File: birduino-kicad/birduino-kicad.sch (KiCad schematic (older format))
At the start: 22 parts, among them J1 Conn_01x03_Male, J2 Conn_01x02_Male, J3 Conn_02x05_Odd_Even, J4 Conn_01x04, Q1 2N7000, Q2 2N7000, Q3 2N7000, SW1 SW_Push_Dual, SW2 SW_Push_Dual, SW3 SW_Push_Dual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

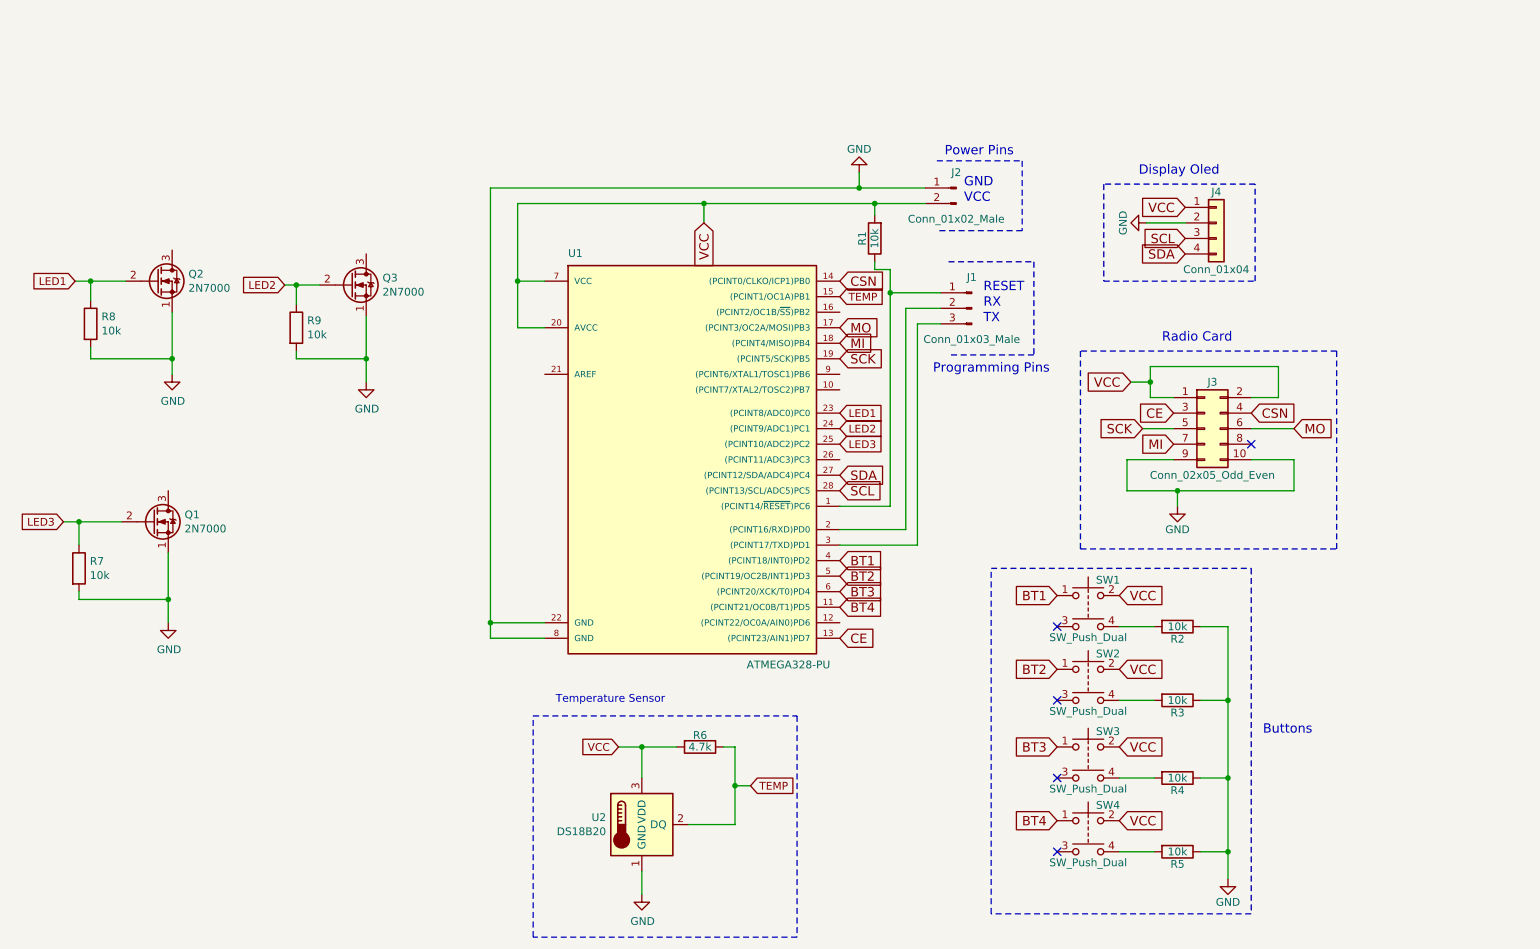
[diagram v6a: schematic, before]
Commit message: feat: add new sensors and components
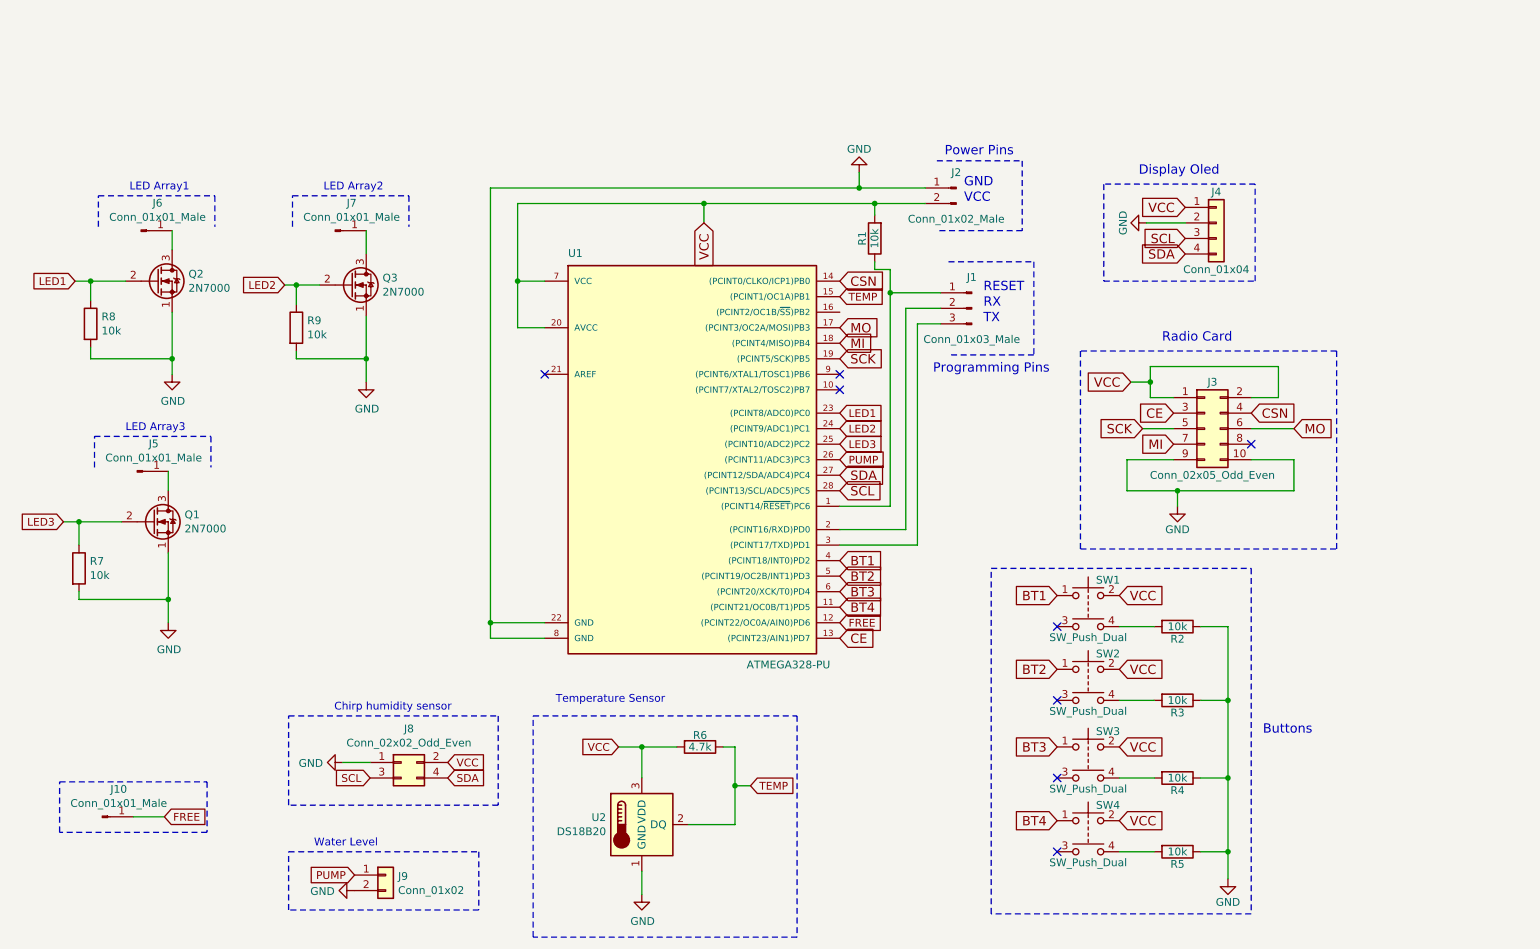
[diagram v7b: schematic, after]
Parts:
- added J10, J5, J6, J7: Conn_01x01_Male, Connector_PinHeader_2.54mm:PinHeader_1x01_P2.54mm_Vertical, symbol Connector:Conn_01x01_Male
- added J8: Conn_02x02_Odd_Even, Connector_PinHeader_2.54mm:PinHeader_2x02_P2.54mm_Vertical, symbol Connector_Generic:Conn_02x02_Odd_Even
- added J9: Conn_01x02, Connector_PinHeader_2.54mm:PinHeader_1x02_P2.54mm_Vertical, symbol Connector_Generic:Conn_01x02
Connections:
- net GND: now also J8.1 (Pin_1), J9.2 (Pin_2)
- net SCL: now also J8.3 (Pin_3)
- net SDA: now also J8.4 (Pin_4)
- net VCC: now also J8.2 (Pin_2)
- net FREE: now reaches U1.12 ((PCINT22/OC0A/AIN0)PD6)
- net FREE: now also J10.1 (Pin_1)
- net PUMP: now reaches U1.26 ((PCINT11/ADC3)PC3)
- net PUMP: now also J9.1 (Pin_1)
- net at Q3.3 (D): now also J7.1 (Pin_1)
- net at Q2.3 (D): now also J6.1 (Pin_1)
- net at Q1.3 (D): now also J5.1 (Pin_1)
- no-connect marks 5 -> 8
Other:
- note added: "Chirp humidity sensor"
- note added: "LED Array1"
- note added: "LED Array2"
- note added: "LED Array3"
- note added: "Water Level"
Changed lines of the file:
@@
 Text GLabel 6525 3275 2    50   Input ~ 0
 LED3
+$Comp
+L Connector:Conn_01x01_Male J6
+U 1 1 5C995BFC
+P 2025 1900
+F 0 "J6" H 2131 2078 50  0000 C CNN
+F 1 "Conn_01x01_Male" H 2131 1987 50  0000 C CNN
+F 2 "Connector_PinHeader_2.54mm:PinHeader_1x01_P2.54mm_Vertical" H 2025 1900 50  0001 C CNN
+F 3 "~" H 2025 1900 50  0001 C CNN
+	1    2025 1900
+	1    0    0    -1
+$EndComp
+$Comp
+L Connector:Conn_01x01_Male J7
+U 1 1 5C9966C3
+P 3275 1900
+F 0 "J7" H 3381 2078 50  0000 C CNN
+F 1 "Conn_01x01_Male" H 3381 1987 50  0000 C CNN
+F 2 "Connector_PinHeader_2.54mm:PinHeader_1x01_P2.54mm_Vertical" H 3275 1900 50  0001 C CNN
+F 3 "~" H 3275 1900 50  0001 C CNN
+	1    3275 1900
+	1    0    0    -1
+$EndComp
+$Comp
+L Connector:Conn_01x01_Male J5
+U 1 1 5C99677B
+P 2000 3450
+F 0 "J5" H 2106 3628 50  0000 C CNN
+F 1 "Conn_01x01_Male" H 2106 3537 50  0000 C CNN
+F 2 "Connector_PinHeader_2.54mm:PinHeader_1x01_P2.54mm_Vertical" H 2000 3450 50  0001 C CNN
+F 3 "~" H 2000 3450 50  0001 C CNN
+	1    2000 3450
+	1    0    0    -1
+$EndComp
+Wire Wire Line
+	2225 2025 2225 1900
+Wire Wire Line
+	3475 2050 3475 1900
+Wire Wire Line
+	2200 3575 2200 3450
+Wire Notes Line
+	1750 1875 1750 1675
+Wire Notes Line
+	1750 1675 2500 1675
+Wire Notes Line
+	2500 1675 2500 1875
+Text Notes 1950 1650 0    50   ~ 0
+LED Array1
+Wire Notes Line
+	3000 1875 3000 1675
+Wire Notes Line
+	3000 1675 3750 1675
+Wire Notes Line
+	3750 1675 3750 1875
+Text Notes 3200 1650 0    50   ~ 0
+LED Array2
+Wire Notes Line
+	1725 3425 1725 3225
+Wire Notes Line
+	1725 3225 2475 3225
+Wire Notes Line
+	2475 3225 2475 3425
+Text Notes 1925 3200 0    50   ~ 0
+LED Array3
+Text GLabel 4000 5325 2    50   Input ~ 0
+VCC
+Text GLabel 3500 5425 0    50   Input ~ 0
+SCL
+Text GLabel 4000 5425 2    50   Input ~ 0
+SDA
+$Comp
+L power:GND #PWR0105
+U 1 1 5C9B4293
+P 3325 5325
+F 0 "#PWR0105" H 3325 5075 50  0001 C CNN
+F 1 "GND" V 3330 5197 50  0000 R CNN
+F 2 "" H 3325 5325 50  0001 C CNN
+F 3 "" H 3325 5325 50  0001 C CNN
+	1    3325 5325
+	0    1    1    0
+$EndComp
+Wire Notes Line
+	2975 5025 4325 5025
+Wire Notes Line
+	4325 5025 4325 5600
+Wire Notes Line
+	4325 5600 2975 5600
+Wire Notes Line
+	2975 5600 2975 5025
+Text Notes 4025 5000 2    50   ~ 0
+Chirp humidity sensor
+$Comp
+L Connector_Generic:Conn_02x02_Odd_Even J8
+U 1 1 5C9C2C91
+P 3700 5325
+F 0 "J8" H 3750 5542 50  0000 C CNN
+F 1 "Conn_02x02_Odd_Even" H 3750 5451 50  0000 C CNN
+F 2 "Connector_PinHeader_2.54mm:PinHeader_2x02_P2.54mm_Vertical" H 3700 5325 50  0001 C CNN
+F 3 "~" H 3700 5325 50  0001 C CNN
+	1    3700 5325
+	1    0    0    -1
+$EndComp
+Wire Wire Line
+	3325 5325 3500 5325
+$Comp
+L Connector_Generic:Conn_01x02 J9
+U 1 1 5C9D2908
+P 3600 6050
+F 0 "J9" H 3680 6042 50  0000 L CNN
+F 1 "Conn_01x02" H 3680 5951 50  0000 L CNN
+F 2 "Connector_PinHeader_2.54mm:PinHeader_1x02_P2.54mm_Vertical" H 3600 6050 50  0001 C CNN
+F 3 "~" H 3600 6050 50  0001 C CNN
+	1    3600 6050
+	1    0    0    -1
+$EndComp
+Text GLabel 3400 6050 0    50   Input ~ 0
+PUMP
+$Comp
+L power:GND #PWR0106
+U 1 1 5C9D2AF1
+P 3400 6150
+F 0 "#PWR0106" H 3400 5900 50  0001 C CNN
+F 1 "GND" V 3405 6022 50  0000 R CNN
+F 2 "" H 3400 6150 50  0001 C CNN
+F 3 "" H 3400 6150 50  0001 C CNN
+	1    3400 6150
+	0    1    1    0
+$EndComp
+Wire Notes Line
+	2975 5900 4200 5900
+Wire Notes Line
+	4200 5900 4200 6275
+Wire Notes Line
+	4200 6275 2975 6275
+Wire Notes Line
+	2975 6275 2975 5900
+Text Notes 3550 5875 2    50   ~ 0
+Water Level
+Text GLabel 6525 3375 2    50   Input ~ 0
+PUMP
+NoConn ~ 4625 2825
+NoConn ~ 6525 2825
+NoConn ~ 6525 2925
+$Comp
+L Connector:Conn_01x01_Male J10
+U 1 1 5C9DF6BE
+P 1775 5675
+F 0 "J10" H 1881 5853 50  0000 C CNN
+F 1 "Conn_01x01_Male" H 1881 5762 50  0000 C CNN
+F 2 "Connector_PinHeader_2.54mm:PinHeader_1x01_P2.54mm_Vertical" H 1775 5675 50  0001 C CNN
+F 3 "~" H 1775 5675 50  0001 C CNN
+	1    1775 5675
+	1    0    0    -1
+$EndComp
+Text GLabel 2175 5675 2    50   Input ~ 0
+FREE
+Wire Wire Line
+	1975 5675 2175 5675
+Text GLabel 6525 4425 2    50   Input ~ 0
+FREE
+Wire Notes Line
+	1500 5450 2450 5450
+Wire Notes Line
+	2450 5450 2450 5775
+Wire Notes Line
+	2450 5775 1500 5775
+Wire Notes Line
+	1500 5775 1500 5450
 $EndSCHEMATC

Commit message: feat: First final version 1.0. 3D image added to readme
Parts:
- added J11: Conn_01x01_Male, Connector_PinHeader_2.54mm:PinHeader_1x01_P2.54mm_Vertical, symbol Connector:Conn_01x01_Male
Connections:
- new net StepUp5V/5V: J11.1 (Pin_1)
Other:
- moved on the sheet: J3, J4, R2, R3, R4, R5, SW1, SW2, SW3, SW4
